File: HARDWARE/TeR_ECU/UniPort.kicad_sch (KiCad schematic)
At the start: 1 part, among them J1 RJ45_Shielded

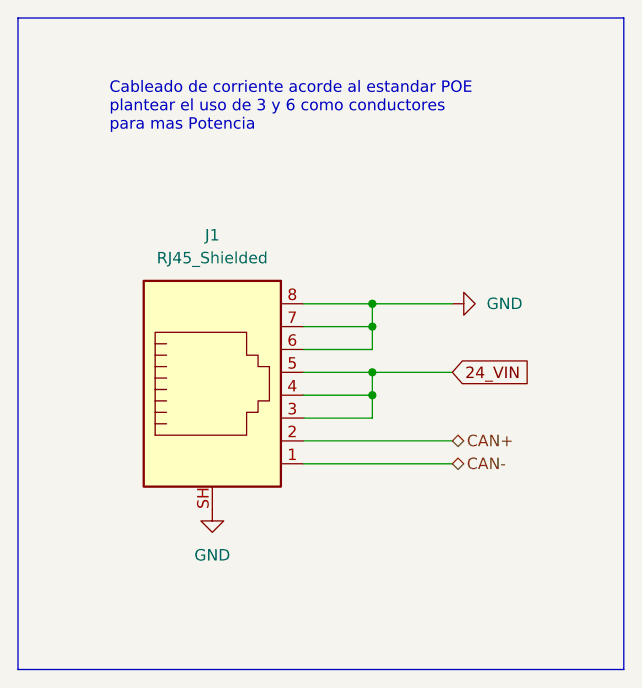
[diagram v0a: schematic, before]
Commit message: Corregidos conectores, CAN y añadidas librerias al proyecto para cargar huellas
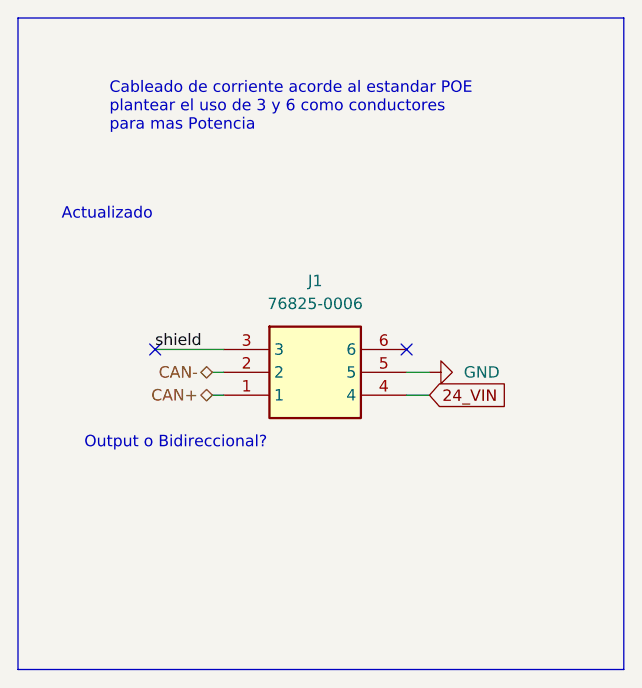
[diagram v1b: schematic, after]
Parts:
- removed J1: RJ45_Shielded, Connector_RJ:RJ45_Ninigi_GE, symbol Connector:RJ45_Shielded
- added J1: 76825-0006, 76825-0006:768250006, symbol 76825-0006:76825-0006
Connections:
- net 24_VIN: now also J1.4
- net CAN+: now also J1.1
- net CAN-: now also J1.2
- net GND: now also J1.5
- new net shield: J1.3
- no-connect marks 0 -> 2
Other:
- note added: "Actualizado"
- note added: "Output o Bidireccional?"
